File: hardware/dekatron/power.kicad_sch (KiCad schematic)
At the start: 94 parts, among them J101 PWR_IN, J102 NIX_12V, Q101 IPD50P04P4L-11, Q102 IPD50R1K4CE, U101 TPS54202, U102 LM66100, U103 LM66100, U104 LM66100, U105 LP2951 (adj. 10 V), U106 LM5156H, U107 TLV3011, U108 TLV3011

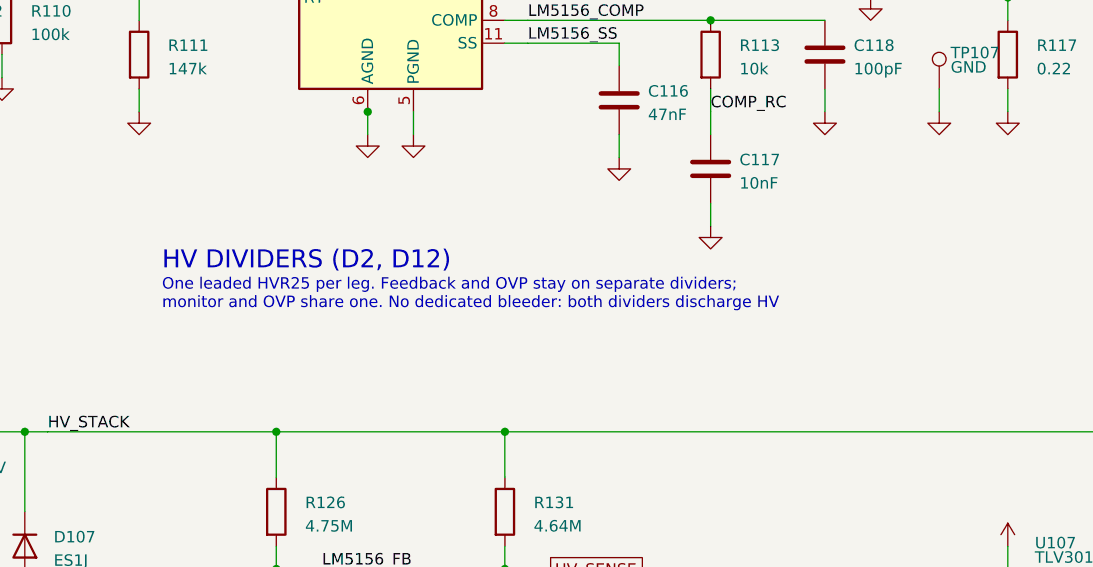
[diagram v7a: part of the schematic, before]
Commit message: Replace Vishay HVR25/HVR37 with Yageo HHV-25/HHV-50 (Mouser stock)
Same ratings (1600 V / 3500 V DC, 1 %, 200 ppm/K, 100k-68M E24/E96) and bodies
no larger (6.3 x 2.4 mm, 9.0 x 3.3 mm), so the 0207/0411 footprints stay.
Generator emits Yageo ordering codes (HHV-25FT-52-4M75 etc.); PCB fields
synced in place, ERC/DRC parity unchanged. hardware.md records the voltage
each leg actually needs at the 1.5x rule: >= 830 V for the two HV divider
tops, >= 415 V / 0.5 W for the anode pair, >= 303 V for the V_b-side parts.

Co-Authored-By: Claude Opus 5.5 <noreply@anthropic.com>
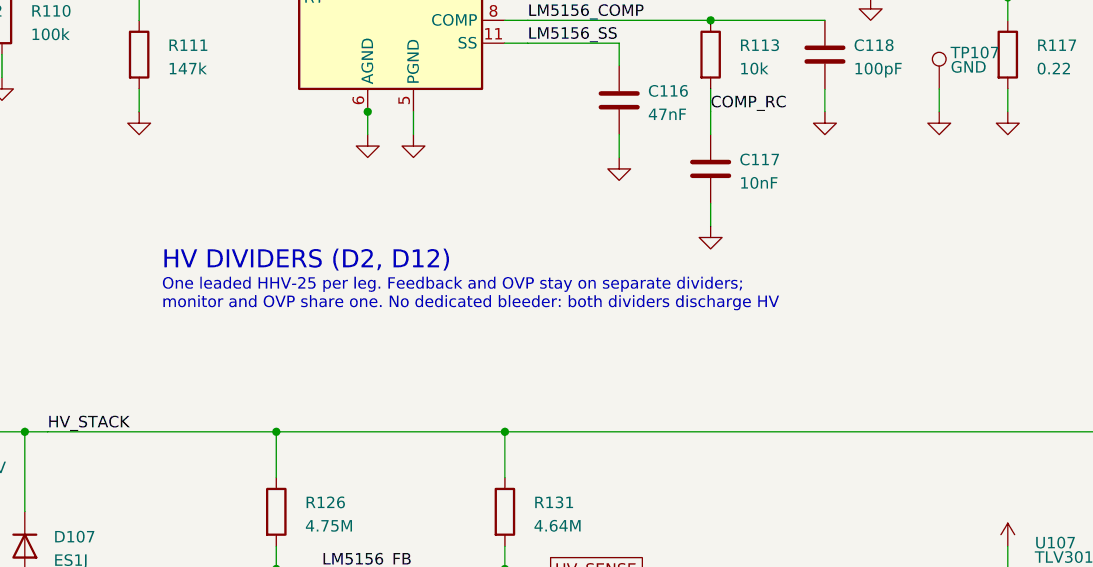
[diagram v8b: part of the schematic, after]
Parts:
- R119: MPN HVR2500002404FR500 -> HHV-25FT-52-2M4; Manufacturer Vishay -> Yageo; Rating HVR25: 0.25 W, 1600 V DC, 1 %, 200 ppm/K -> HHV-25: 0.25 W, 1600 V DC, 1 %, 200 ppm/K
- R126: MPN HVR2500004754FR500 -> HHV-25FT-52-4M75; Manufacturer Vishay -> Yageo; Rating HVR25: 0.25 W, 1600 V DC, 1 %, 200 ppm/K -> HHV-25: 0.25 W, 1600 V DC, 1 %, 200 ppm/K
- R131: MPN HVR2500004644FR500 -> HHV-25FT-52-4M64; Manufacturer Vishay -> Yageo; Rating HVR25: 0.25 W, 1600 V DC, 1 %, 200 ppm/K -> HHV-25: 0.25 W, 1600 V DC, 1 %, 200 ppm/K
- R141: MPN HVR2500002004FR500 -> HHV-25FT-52-2M; Manufacturer Vishay -> Yageo; Rating HVR25: 0.25 W, 1600 V DC, 1 %, 200 ppm/K -> HHV-25: 0.25 W, 1600 V DC, 1 %, 200 ppm/K
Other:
- note added: "One leaded HHV-25 per leg. Feedback and OVP stay on separate dividers; monitor and OVP share one. No dedicated bleeder: both dividers discharge HV"
- note removed: "One leaded HVR25 per leg. Feedback and OVP stay on separate dividers; monitor and OVP share one. No dedicated bleeder: both dividers discharge HV"
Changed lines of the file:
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@@
 	  (property "Description" "Resistor" (at 276.86 171.45 0) (hide yes) (show_name no) (do_not_autoplace no) (effects (font (size 1.27 1.27)) (justify left)))
 	  (property "Function" "V_b bleeder (V_b's own discharge path with L3 open)" (at 276.86 171.45 0) (hide yes) (show_name no) (do_not_autoplace no) (effects (font (size 1.27 1.27)) (justify left)))
-	  (property "MPN" "HVR2500002404FR500" (at 276.86 171.45 0) (hide yes) (show_name no) (do_not_autoplace no) (effects (font (size 1.27 1.27)) (justify left)))
-	  (property "Manufacturer" "Vishay" (at 276.86 171.45 0) (hide yes) (show_name no) (do_not_autoplace no) (effects (font (size 1.27 1.27)) (justify left)))
-	  (property "Rating" "HVR25: 0.25 W, 1600 V DC, 1 %, 200 ppm/K" (at 276.86 171.45 0) (hide yes) (show_name no) (do_not_autoplace no) (effects (font (size 1.27 1.27)) (justify left)))
+	  (property "MPN" "HHV-25FT-52-2M4" (at 276.86 171.45 0) (hide yes) (show_name no) (do_not_autoplace no) (effects (font (size 1.27 1.27)) (justify left)))
+	  (property "Manufacturer" "Yageo" (at 276.86 171.45 0) (hide yes) (show_name no) (do_not_autoplace no) (effects (font (size 1.27 1.27)) (justify left)))
+	  (property "Rating" "HHV-25: 0.25 W, 1600 V DC, 1 %, 200 ppm/K" (at 276.86 171.45 0) (hide yes) (show_name no) (do_not_autoplace no) (effects (font (size 1.27 1.27)) (justify left)))
 	  (pin "1")
 	  (pin "2")
@@
 	  (property "Description" "Resistor" (at 297.18 171.45 0) (hide yes) (show_name no) (do_not_autoplace no) (effects (font (size 1.27 1.27)) (justify left)))
 	  (property "Function" "V_b OVP divider, upper" (at 297.18 171.45 0) (hide yes) (show_name no) (do_not_autoplace no) (effects (font (size 1.27 1.27)) (justify left)))
-	  (property "MPN" "HVR2500002004FR500" (at 297.18 171.45 0) (hide yes) (show_name no) (do_not_autoplace no) (effects (font (size 1.27 1.27)) (justify left)))
-	  (property "Manufacturer" "Vishay" (at 297.18 171.45 0) (hide yes) (show_name no) (do_not_autoplace no) (effects (font (size 1.27 1.27)) (justify left)))
-	  (property "Rating" "HVR25: 0.25 W, 1600 V DC, 1 %, 200 ppm/K" (at 297.18 171.45 0) (hide yes) (show_name no) (do_not_autoplace no) (effects (font (size 1.27 1.27)) (justify left)))
+	  (property "MPN" "HHV-25FT-52-2M" (at 297.18 171.45 0) (hide yes) (show_name no) (do_not_autoplace no) (effects (font (size 1.27 1.27)) (justify left)))
+	  (property "Manufacturer" "Yageo" (at 297.18 171.45 0) (hide yes) (show_name no) (do_not_autoplace no) (effects (font (size 1.27 1.27)) (justify left)))
+	  (property "Rating" "HHV-25: 0.25 W, 1600 V DC, 1 %, 200 ppm/K" (at 297.18 171.45 0) (hide yes) (show_name no) (do_not_autoplace no) (effects (font (size 1.27 1.27)) (justify left)))
 	  (pin "1")
 	  (pin "2")
@@
 	(label "TRP_P2" (at 106.68 276.86 0) (effects (font (size 1.27 1.27)) (justify left bottom)))
 	(text "HV DIVIDERS (D2, D12)" (exclude_from_sim no) (at 139.7 233.68 0) (effects (font (size 2.0 2.0)) (justify left bottom)))
-	(text "One leaded HVR25 per leg. Feedback and OVP stay on separate dividers;\nmonitor and OVP share one. No dedicated bleeder: both dividers discharge HV" (exclude_from_sim no) (at 139.7 238 0) (effects (font (size 1.27 1.27)) (justify left bottom)))
+	(text "One leaded HHV-25 per leg. Feedback and OVP stay on separate dividers;\nmonitor and OVP share one. No dedicated bleeder: both dividers discharge HV" (exclude_from_sim no) (at 139.7 238 0) (effects (font (size 1.27 1.27)) (justify left bottom)))
 	(wire (pts (xy 152.4 251.46) (xy 152.4 256.54)) (stroke (width 0) (type default)))
 	(symbol (lib_id "Device:R") (at 152.4 260.35 0) (unit 1) (body_style 1) (exclude_from_sim no) (in_bom yes) (on_board yes) (in_pos_files yes) (dnp no)
@@
 	  (property "Description" "Resistor" (at 152.4 260.35 0) (hide yes) (show_name no) (do_not_autoplace no) (effects (font (size 1.27 1.27)) (justify left)))
 	  (property "Function" "HV feedback divider, upper" (at 152.4 260.35 0) (hide yes) (show_name no) (do_not_autoplace no) (effects (font (size 1.27 1.27)) (justify left)))
-	  (property "MPN" "HVR2500004754FR500" (at 152.4 260.35 0) (hide yes) (show_name no) (do_not_autoplace no) (effects (font (size 1.27 1.27)) (justify left)))
-	  (property "Manufacturer" "Vishay" (at 152.4 260.35 0) (hide yes) (show_name no) (do_not_autoplace no) (effects (font (size 1.27 1.27)) (justify left)))
-	  (property "Rating" "HVR25: 0.25 W, 1600 V DC, 1 %, 200 ppm/K" (at 152.4 260.35 0) (hide yes) (show_name no) (do_not_autoplace no) (effects (font (size 1.27 1.27)) (justify left)))
+	  (property "MPN" "HHV-25FT-52-4M75" (at 152.4 260.35 0) (hide yes) (show_name no) (do_not_autoplace no) (effects (font (size 1.27 1.27)) (justify left)))
+	  (property "Manufacturer" "Yageo" (at 152.4 260.35 0) (hide yes) (show_name no) (do_not_autoplace no) (effects (font (size 1.27 1.27)) (justify left)))
+	  (property "Rating" "HHV-25: 0.25 W, 1600 V DC, 1 %, 200 ppm/K" (at 152.4 260.35 0) (hide yes) (show_name no) (do_not_autoplace no) (effects (font (size 1.27 1.27)) (justify left)))
 	  (pin "1")
 	  (pin "2")
@@
 	  (property "Description" "Resistor" (at 177.8 260.35 0) (hide yes) (show_name no) (do_not_autoplace no) (effects (font (size 1.27 1.27)) (justify left)))
 	  (property "Function" "HV monitor / OVP divider, upper" (at 177.8 260.35 0) (hide yes) (show_name no) (do_not_autoplace no) (effects (font (size 1.27 1.27)) (justify left)))
-	  (property "MPN" "HVR2500004644FR500" (at 177.8 260.35 0) (hide yes) (show_name no) (do_not_autoplace no) (effects (font (size 1.27 1.27)) (justify left)))
-	  (property "Manufacturer" "Vishay" (at 177.8 260.35 0) (hide yes) (show_name no) (do_not_autoplace no) (effects (font (size 1.27 1.27)) (justify left)))
-	  (property "Rating" "HVR25: 0.25 W, 1600 V DC, 1 %, 200 ppm/K" (at 177.8 260.35 0) (hide yes) (show_name no) (do_not_autoplace no) (effects (font (size 1.27 1.27)) (justify left)))
-	  (pin "1")
-	  (pin "2")
+	  (property "MPN" "HHV-25FT-52-4M64" (at 177.8 260.35 0) (hide yes) (show_name no) (do_not_autoplace no) (effects (font (size 1.27 1.27)) (justify left)))
+	  (property "Manufacturer" "Yageo" (at 177.8 260.35 0) (hide yes) (show_name no) (do_not_autoplace no) (effects (font (size 1.27 1.27)) (justify left)))
+	  (property "Rating" "HHV-25: 0.25 W, 1600 V DC, 1 %, 200 ppm/K" (at 177.8 260.35 0) (hide yes) (show_name no) (do_not_autoplace no) (effects (font (size 1.27 1.27)) (justify left)))
+	  (pin "1")
+	  (pin "2")
